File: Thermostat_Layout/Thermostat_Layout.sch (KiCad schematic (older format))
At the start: 0 parts

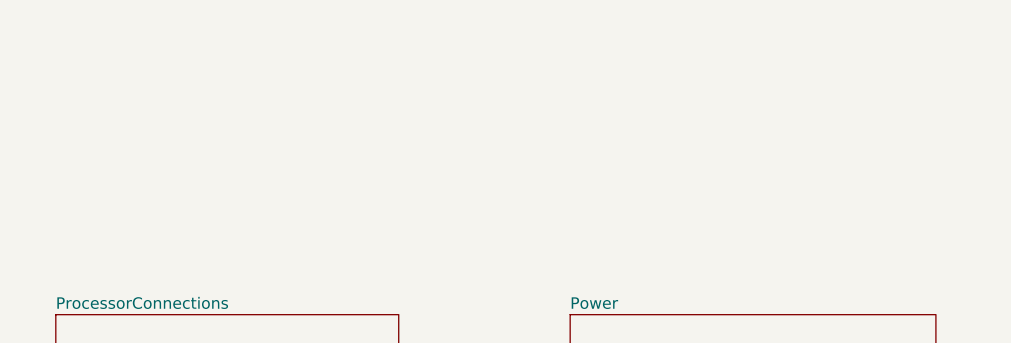
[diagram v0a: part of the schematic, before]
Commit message: Schematic and PCB layout for thermostat
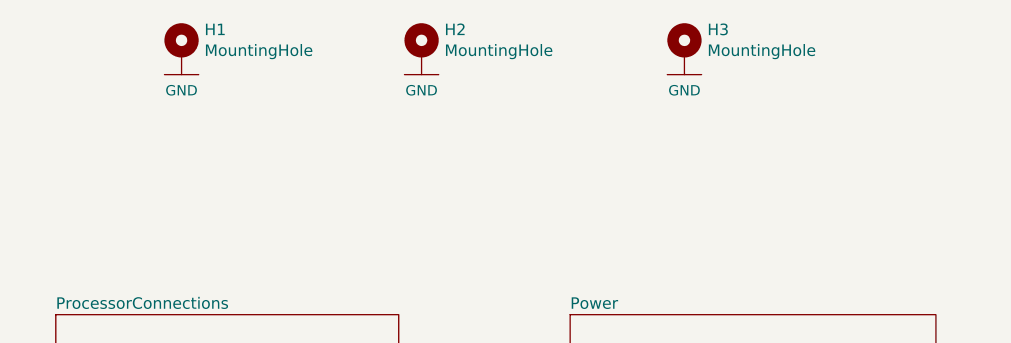
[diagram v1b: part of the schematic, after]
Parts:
- added H1, H2, H3: MountingHole, MountingHole:MountingHole_2.2mm_M2_DIN965_Pad, symbol Mechanical:MountingHole
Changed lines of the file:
@@
 F1 "Radio.sch" 50
 $EndSheet
+$Comp
+L Mechanical:MountingHole H1
+U 1 1 5DB844FC
+P 3150 1100
+F 0 "H1" H 3250 1146 50  0000 L CNN
+F 1 "MountingHole" H 3250 1055 50  0000 L CNN
+F 2 "MountingHole:MountingHole_2.2mm_M2_DIN965_Pad" H 3150 1100 50  0001 C CNN
+F 3 "~" H 3150 1100 50  0001 C CNN
+	1    3150 1100
+	1    0    0    -1
+$EndComp
+$Comp
+L Mechanical:MountingHole H2
+U 1 1 5DB848B5
+P 4200 1100
+F 0 "H2" H 4300 1146 50  0000 L CNN
+F 1 "MountingHole" H 4300 1055 50  0000 L CNN
+F 2 "MountingHole:MountingHole_2.2mm_M2_DIN965_Pad" H 4200 1100 50  0001 C CNN
+F 3 "~" H 4200 1100 50  0001 C CNN
+	1    4200 1100
+	1    0    0    -1
+$EndComp
+$Comp
+L Mechanical:MountingHole H3
+U 1 1 5DB84D49
+P 5350 1100
+F 0 "H3" H 5450 1146 50  0000 L CNN
+F 1 "MountingHole" H 5450 1055 50  0000 L CNN
+F 2 "MountingHole:MountingHole_2.2mm_M2_DIN965_Pad" H 5350 1100 50  0001 C CNN
+F 3 "~" H 5350 1100 50  0001 C CNN
+	1    5350 1100
+	1    0    0    -1
+$EndComp
+$Comp
+L SparkFun-PowerSymbols:GND #GND0102
+U 1 1 5DB857A9
+P 3150 1150
+F 0 "#GND0102" H 3200 1100 45  0001 L BNN
+F 1 "GND" H 3150 980 45  0000 C CNN
+F 2 "" H 3150 1050 60  0001 C CNN
+F 3 "" H 3150 1050 60  0001 C CNN
+	1    3150 1150
+	1    0    0    -1
+$EndComp
+$Comp
+L SparkFun-PowerSymbols:GND #GND0103
+U 1 1 5DB85A7D
+P 4200 1150
+F 0 "#GND0103" H 4250 1100 45  0001 L BNN
+F 1 "GND" H 4200 980 45  0000 C CNN
+F 2 "" H 4200 1050 60  0001 C CNN
+F 3 "" H 4200 1050 60  0001 C CNN
+	1    4200 1150
+	1    0    0    -1
+$EndComp
+$Comp
+L SparkFun-PowerSymbols:GND #GND0104
+U 1 1 5DB85D81
+P 5350 1150
+F 0 "#GND0104" H 5400 1100 45  0001 L BNN
+F 1 "GND" H 5350 980 45  0000 C CNN
+F 2 "" H 5350 1050 60  0001 C CNN
+F 3 "" H 5350 1050 60  0001 C CNN
+	1    5350 1150
+	1    0    0    -1
+$EndComp
 $EndSCHEMATC
